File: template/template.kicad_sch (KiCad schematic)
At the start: 3 parts, among them J1 B2B STLink connector, U1 STM32G474RBT6

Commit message: Schematics for the first version of the STM32 template
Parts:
- added C1, C10, C11, C12, C14, C17, C3, C6, C9: 100n, symbol Device:C
- added C13: 4.7u, symbol Device:C
- added C15, C16: 30p, symbol Device:C
- added C2, C4, C5, C8: 1u, symbol Device:C
- added C7: 10n, symbol Device:C
- added D1: GREEN, symbol Device:LED
- added D2: YELLOW, symbol Device:LED
- added F1: 2A, symbol Device:Fuse
- added H1, H2, H3, H4: 2.7mm, MountingHole:MountingHole_2.7mm_Pad, symbol Mechanical:MountingHole_Pad
- added J1: Network Connector, symbol Exocet:Network_Connector
- added R2: 40, symbol Device:R
- added R3: 120, Resistor_THT:R_Axial_DIN0309_L9.0mm_D3.2mm_P12.70mm_Horizontal, symbol Device:R
- added R4: 80, symbol Device:R
- added R5: 10k, symbol Device:R
- added SW1: SW_Push, Button_Switch_THT:SW_PUSH_6mm, symbol Switch:SW_Push
- added TP1, TP2, TP3, TP4, TP5: TestPoint, TestPoint:TestPoint_Keystone_5005-5009_Compact, symbol Connector:TestPoint
- added U1: LD39050PU33R, Package_DFN_QFN:DFN-6-1EP_3x3mm_P0.95mm_EP1.7x2.6mm, symbol Exocet:LD39050PU33R
- added U3: SN65HVD230, Package_SO:SOIC-8_3.9x4.9mm_P1.27mm, symbol Interface_CAN_LIN:SN65HVD230
- added Y1: 8MHz, symbol Exocet:HSE_Oscillator
- J2: renamed from J1; footprint Exocet_Footprint:AVX 00-9159-010-BTB Connector -> Exocet:AVX 00-9159-010-BTB Connector; now not fitted
- R1: value 47Ω -> 47
- renumbered U1 to U2
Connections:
- net +3.3V: now also U2.1 (VBAT), U2.16 (VDD), U2.28 (VREF+), U2.29 (VDDA), U2.32 (VDD), U2.48 (VDD), U2.64 (VDD), C10.1, C11.1, C12.1, C13.1, C17.1, C2.2, C3.2, C5.1, C6.1, C7.1, C8.1, C9.1, R2.1, TP5.1, U1.4 (V_{out}), U3.3 (VCC)
- net GND: now also U2.15 (VSS), U2.27 (VSSA), U2.31 (VSS), U2.47 (VSS), U2.63 (VSS), C1.2, C10.2, C11.2, C12.2, C13.2, C14.1, C15.2, C16.2, C17.2, C2.1, C3.1, C4.2, C5.2, C6.2, C7.2, C8.2, C9.2, D1.1 (K), D2.1 (K), H1.1, H2.1, H3.1, H4.1, J1.5 (GND), R5.2, SW1.1, TP1.1, U1.2 (GND), U1.7 (GND), U3.2 (GND)
- net T_NRST: now also C14.2, SW1.2
- net CAN_RX: now reaches U2.45 (PA11)
- net CAN_RX: now also TP2.1, U3.4 (R)
- net CAN_TX: now reaches U2.46 (PA12)
- net CAN_TX: now also TP4.1, U3.1 (D)
- net OSC_IN: now reaches U2.5 (PF0)
- net OSC_IN: now also C15.1, Y1.1
- net OSC_OUT: now reaches U2.6 (PF1)
- net OSC_OUT: now also C16.1, Y1.2
- net STATUS_LED: now reaches U2.8 (PC0)
- net STATUS_LED: now also R4.1
- new net: F1.1, J1.2 (+5V)
- new net: D1.2 (A), R2.2
- new net: R5.1, U3.8 (Rs)
- new net: D2.2 (A), R4.2
- new net +24V: J1.1 (+24V)
- new net +5V: C1.1, C4.1, F1.2, TP3.1, U1.1 (EN), U1.6 (V_{in})
- new net CAN_H: J1.3 (CAN_H), R3.2, U3.7 (CANH)
- new net CAN_L: J1.4 (CAN_L), R3.1, U3.6 (CANL)
- no-connect marks 1 -> 43
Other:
- note added: "CAN Tranceiver"
- note added: "Mounting Holes"
- note added: "Network Connector"
- note added: "Oscillator"
- note added: "Reset Button"
- note added: "STLink"
- note added: "STM32"
- note added: "Status LEDs"
- note added: "Termination Resistor"
- note added: "Test Points"
- note added: "Voltage Regulator"
- moved on the sheet: R1, U2

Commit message: Add oscillator symbol
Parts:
- Y1: footprint (none) -> Exocet:Crystal_SMD_HC49-SD
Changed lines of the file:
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@@
 			)
 		)
-		(property "Footprint" ""
+		(property "Footprint" "Exocet:Crystal_SMD_HC49-SD"
 			(at 200.66 25.4 0)
 			(effects

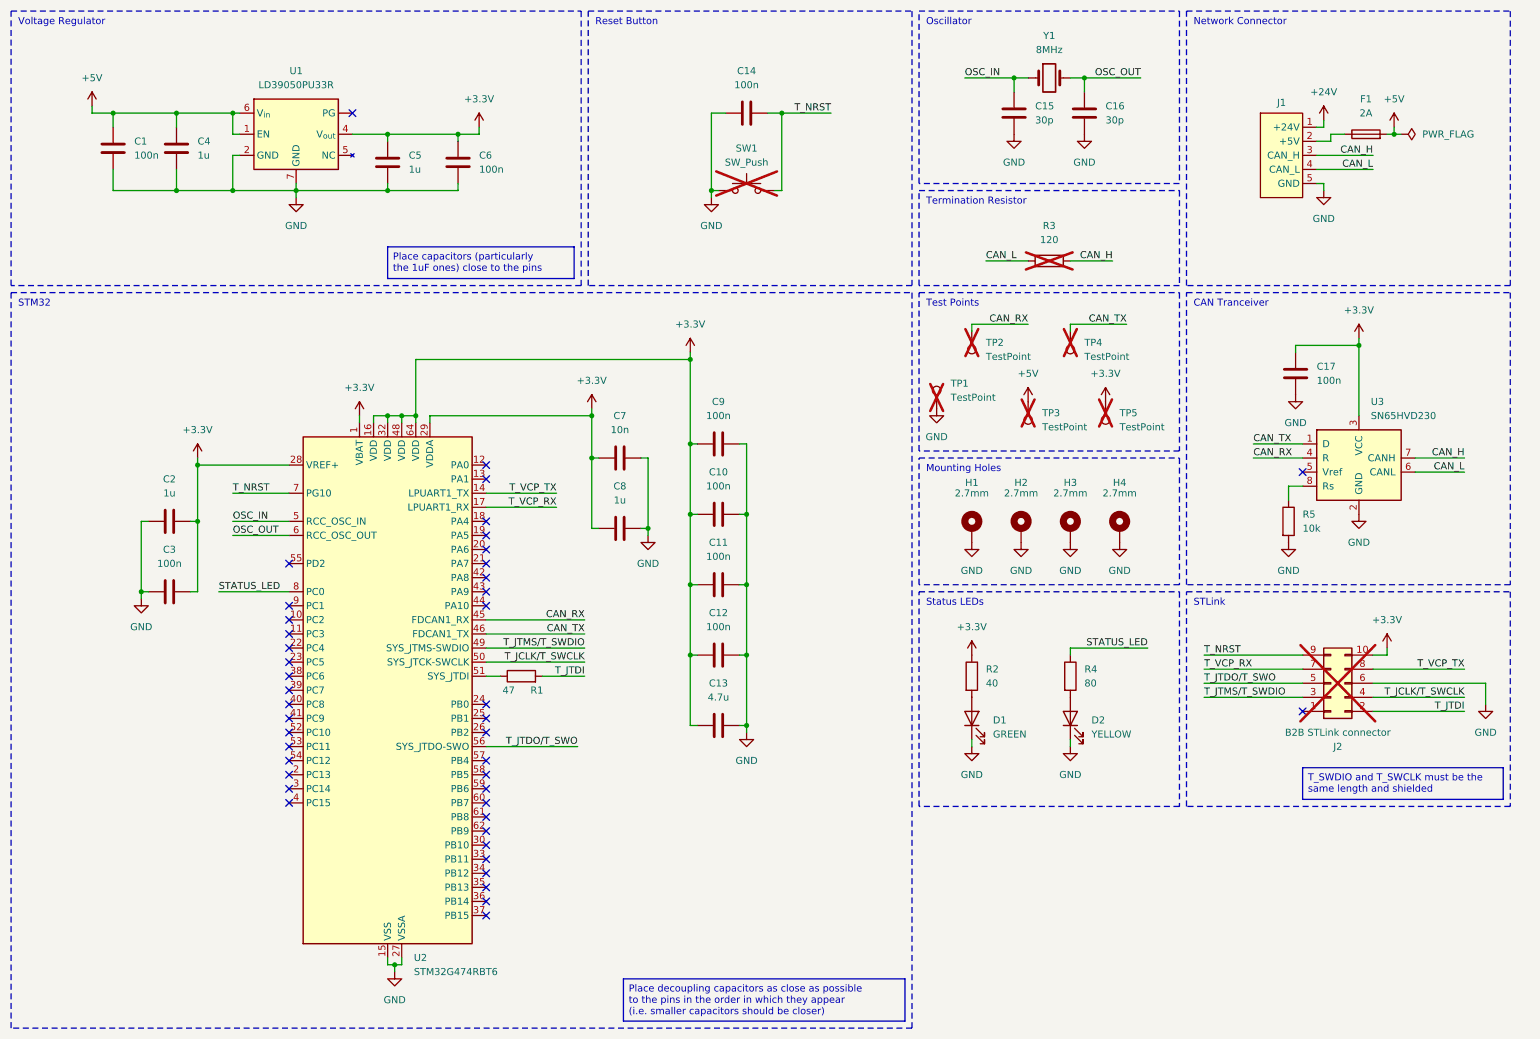
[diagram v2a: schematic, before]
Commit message: Footprints and part numbers
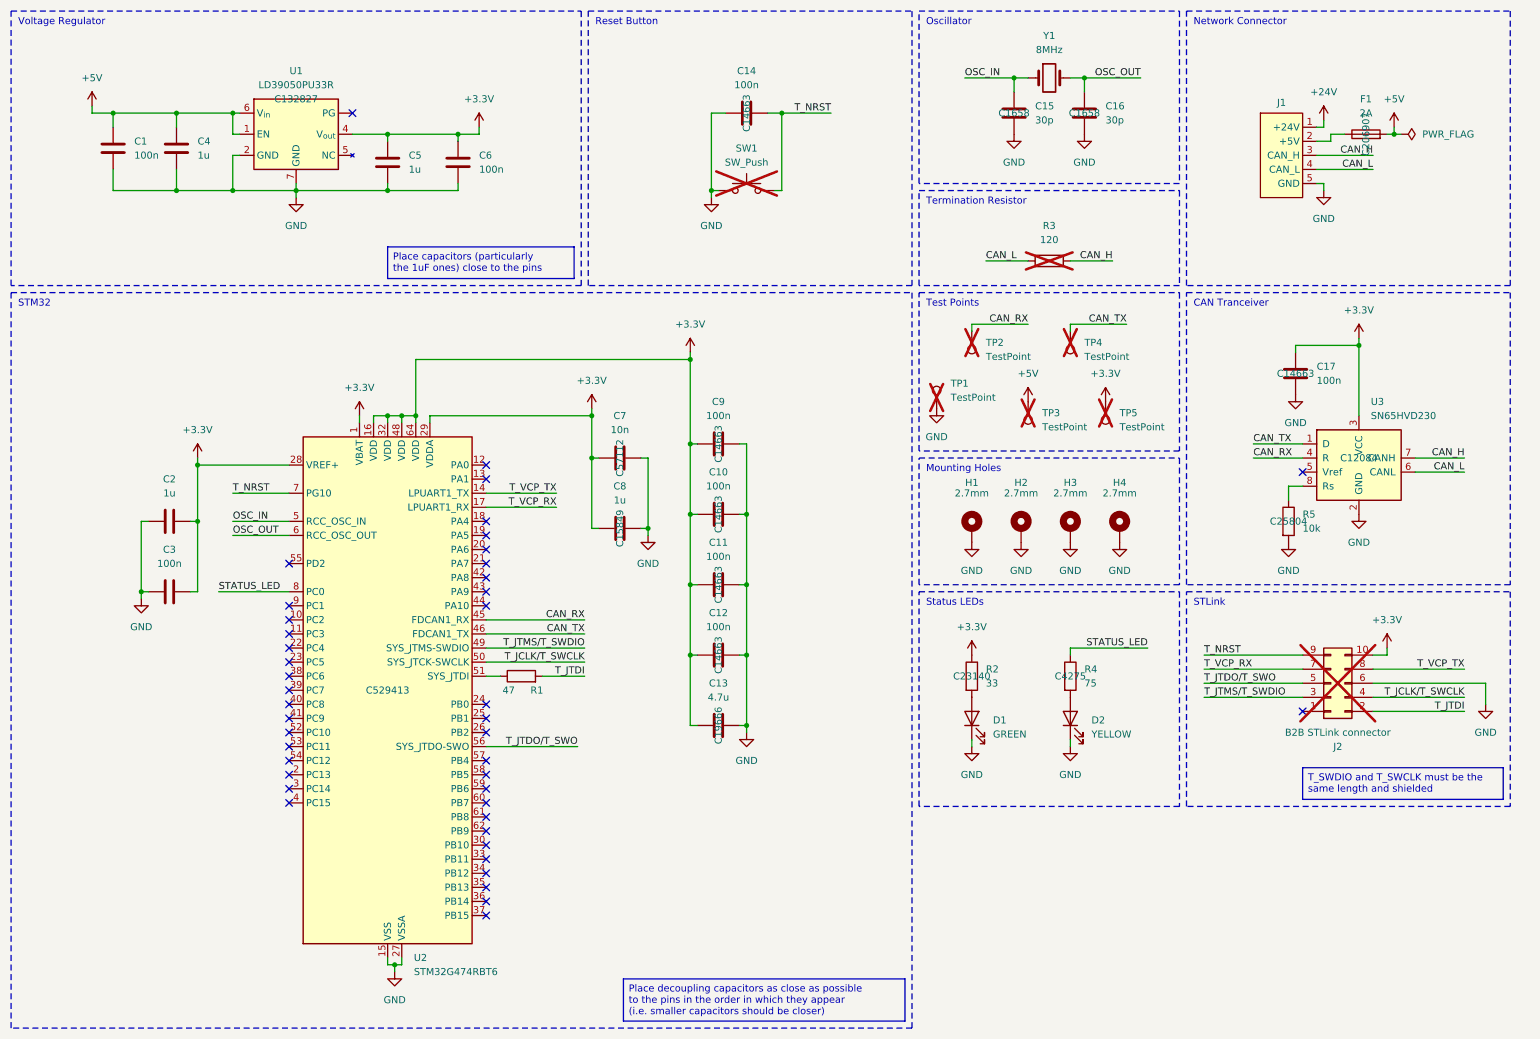
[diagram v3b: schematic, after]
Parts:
- C1, C10, C11, C12, C14, C17, C3, C6, C9: footprint (none) -> Capacitor_SMD:C_0603_1608Metric; JLCPCB (none) -> C14663
- C13: footprint (none) -> Capacitor_SMD:C_0603_1608Metric; JLCPCB (none) -> C19666
- C15, C16: footprint (none) -> Capacitor_SMD:C_0603_1608Metric; JLCPCB (none) -> C1658
- C2, C4, C5, C8: footprint (none) -> Capacitor_SMD:C_0603_1608Metric; JLCPCB (none) -> C15849
- C7: footprint (none) -> Capacitor_SMD:C_0603_1608Metric; JLCPCB (none) -> C57112
- D1: footprint (none) -> Exocet:LED_0805_2012Metric_With_Annotations; JLCPCB (none) -> C2297
- D2: footprint (none) -> Exocet:LED_0805_2012Metric_With_Annotations; JLCPCB (none) -> C2296
- F1: footprint (none) -> Exocet:Fuse_Holder_Littelfuse_01530008; JLCPCB (none) -> C206907
- J1: footprint (none) -> Connector_Molex:Molex_SPOX_5268-05A_1x05_P2.50mm_Horizontal; JLCPCB (none) -> C185201
- R1: footprint (none) -> Resistor_SMD:R_0603_1608Metric; JLCPCB (none) -> C23182
- R2: value 40 -> 33; footprint (none) -> Resistor_SMD:R_0603_1608Metric; JLCPCB (none) -> C23140
- R4: value 80 -> 75; footprint (none) -> Resistor_SMD:R_0603_1608Metric; JLCPCB (none) -> C4275
- R5: footprint (none) -> Resistor_SMD:R_0603_1608Metric; JLCPCB (none) -> C25804
- U1: JLCPCB (none) -> C132827
- U2: JLCPCB (none) -> C529413
- U3: JLCPCB (none) -> C12084

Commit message: Initial placement and routing
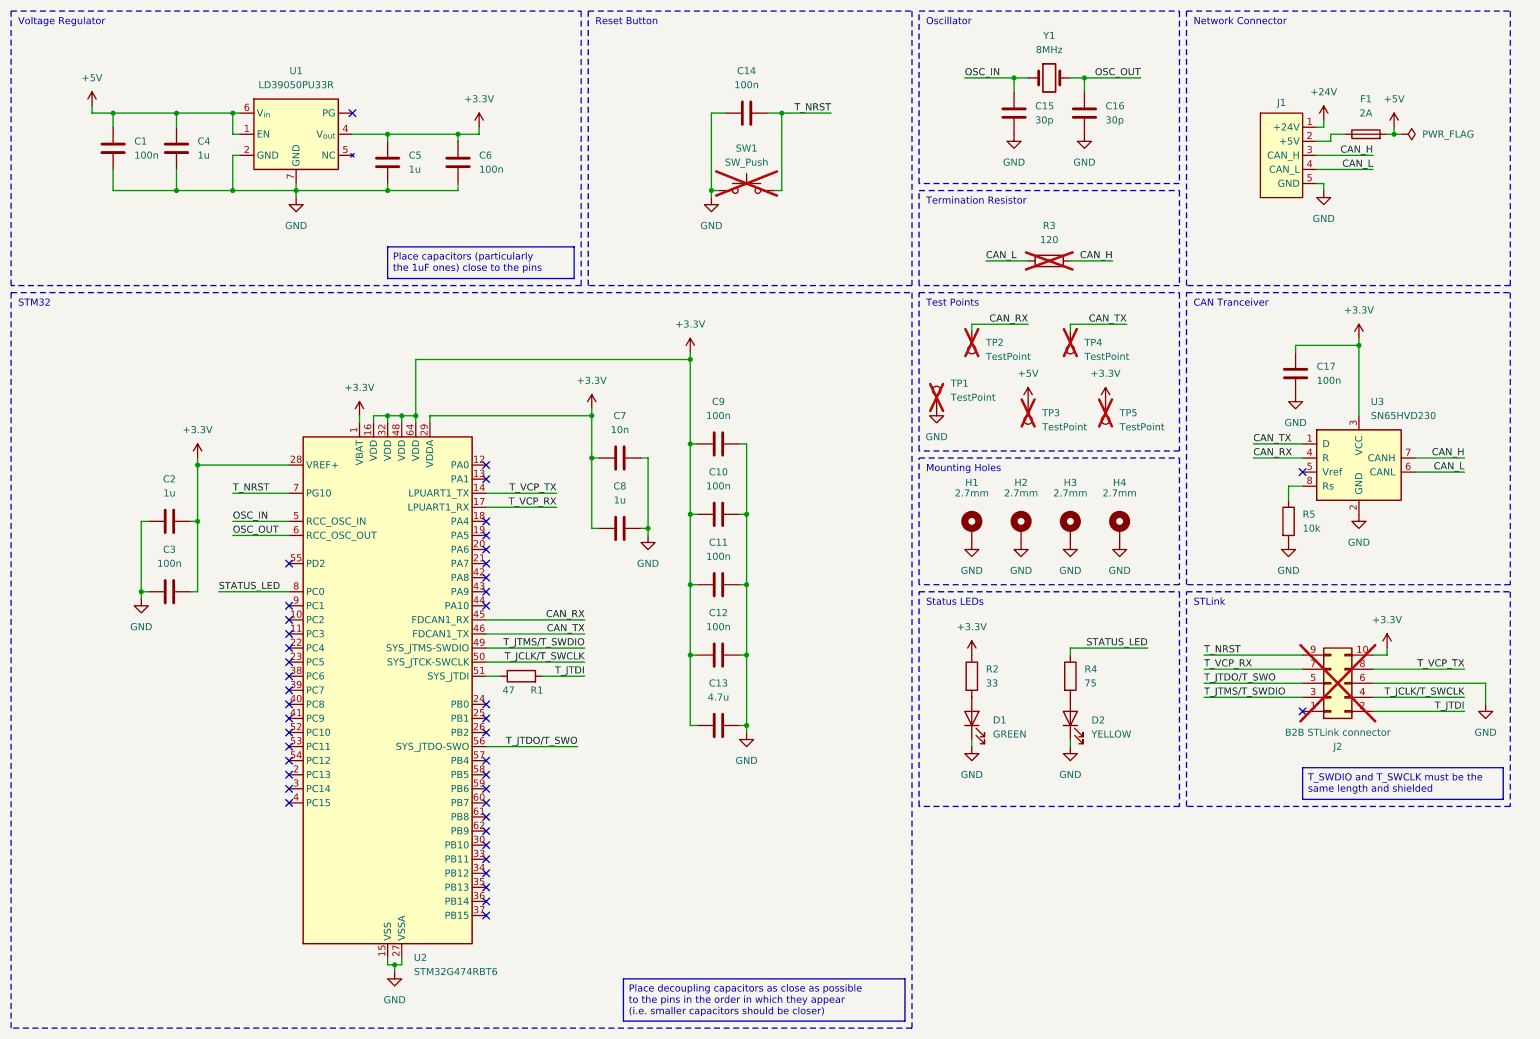
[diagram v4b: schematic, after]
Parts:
- C1, C10, C11, C12, C14, C17, C3, C6, C9: footprint Capacitor_SMD:C_0603_1608Metric -> Capacitor_SMD:C_0402_1005Metric; JLCPCB C14663 -> C1525
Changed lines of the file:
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@@
 					(size 1.27 1.27)
 				)
+				(hide yes)
 			)
 		)
@@
 					(size 1.27 1.27)
 				)
+				(hide yes)
 			)
 		)
@@
 					(size 1.27 1.27)
 				)
+				(hide yes)
 			)
 		)
@@
 			)
 		)
-		(property "Footprint" "Capacitor_SMD:C_0603_1608Metric"
+		(property "Footprint" "Capacitor_SMD:C_0402_1005Metric"
 			(at 45.72 117.1448 0)
 			(effects
@@
 			)
 		)
-		(property "JLCPCB" "C14663"
+		(property "JLCPCB" " C1525"
 			(at 41.91 118.11 0)
 			(effects
@@
 			)
 		)
-		(property "Footprint" "Capacitor_SMD:C_0603_1608Metric"
+		(property "Footprint" "Capacitor_SMD:C_0402_1005Metric"
 			(at 32.7152 41.91 0)
 			(effects
@@
 			)
 		)
-		(property "JLCPCB" "C14663"
+		(property "JLCPCB" " C1525"
 			(at 31.75 38.1 0)
 			(effects
@@
 					(size 1.27 1.27)
 				)
+				(hide yes)
 			)
 		)
@@
 					(size 1.27 1.27)
 				)
+				(hide yes)
 			)
 		)
@@
 			)
 		)
-		(property "Footprint" "Capacitor_SMD:C_0603_1608Metric"
+		(property "Footprint" "Capacitor_SMD:C_0402_1005Metric"
 			(at 144.78 115.8748 0)
 			(effects
@@
 			)
 		)
-		(property "JLCPCB" "C14663"
+		(property "JLCPCB" " C1525"
 			(at 140.97 116.84 0)
 			(effects
@@
 					(size 1.27 1.27)
 				)
+				(hide yes)
 			)
 		)
@@
 			)
 		)
-		(property "Footprint" "Capacitor_SMD:C_0603_1608Metric"
+		(property "Footprint" "Capacitor_SMD:C_0402_1005Metric"
 			(at 94.9452 44.45 0)
 			(effects
@@
 			)
 		)
-		(property "JLCPCB" "C14663"
+		(property "JLCPCB" " C1525"
 			(at 93.98 40.64 0)
 			(effects
@@
 					(size 1.27 1.27)
 				)
+				(hide yes)
 			)
 		)
@@
 					(size 1.27 1.27)
 				)
+				(hide yes)
 			)
 		)
@@
 					(size 1.27 1.27)
 				)
+				(hide yes)
 			)
 		)
@@
 			)
 		)
-		(property "Footprint" "Capacitor_SMD:C_0603_1608Metric"
+		(property "Footprint" "Capacitor_SMD:C_0402_1005Metric"
 			(at 144.78 103.1748 0)
 			(effects
@@
 			)
 		)
-		(property "JLCPCB" "C14663"
+		(property "JLCPCB" " C1525"
 			(at 140.97 104.14 0)
 			(effects
@@
 					(size 1.27 1.27)
 				)
+				(hide yes)
 			)
 		)
@@
 					(size 1.27 1.27)
 				)
+				(hide yes)
 			)
 		)
@@
 					(size 1.27 1.27)
 				)
+				(hide yes)
 			)
 		)
@@
 			)
 		)
-		(property "Footprint" "Capacitor_SMD:C_0603_1608Metric"
+		(property "Footprint" "Capacitor_SMD:C_0402_1005Metric"
 			(at 149.86 30.7848 0)
 			(effects
@@
 			)
 		)
-		(property "JLCPCB" "C14663"
+		(property "JLCPCB" " C1525"
 			(at 146.05 31.75 0)
 			(effects
@@
 					(size 1.27 1.27)
 				)
+				(hide yes)
 			)
 		)
@@
 					(size 1.27 1.27)
 				)
+				(hide yes)
 			)
 		)
@@
 			)
 		)
-		(property "Footprint" "Capacitor_SMD:C_0603_1608Metric"
+		(property "Footprint" "Capacitor_SMD:C_0402_1005Metric"
 			(at 246.0752 82.55 0)
 			(effects
@@
 			)
 		)
-		(property "JLCPCB" "C14663"
+		(property "JLCPCB" " C1525"
 			(at 245.11 78.74 0)
 			(effects
@@
 					(size 1.27 1.27)
 				)
+				(hide yes)
 			)
 		)
@@
 			)
 		)
-		(property "Footprint" "Capacitor_SMD:C_0603_1608Metric"
+		(property "Footprint" "Capacitor_SMD:C_0402_1005Metric"
 			(at 144.78 128.5748 0)
 			(effects
@@
 			)
 		)
-		(property "JLCPCB" "C14663"
+		(property "JLCPCB" " C1525"
 			(at 140.97 129.54 0)
 			(effects
@@
 					(size 1.27 1.27)
 				)
+				(hide yes)
 			)
 		)
@@
 			)
 		)
-		(property "Footprint" "Capacitor_SMD:C_0603_1608Metric"
+		(property "Footprint" "Capacitor_SMD:C_0402_1005Metric"
 			(at 144.78 90.4748 0)
 			(effects
@@
 			)
 		)
-		(property "JLCPCB" "C14663"
+		(property "JLCPCB" " C1525"
 			(at 140.97 91.44 0)
 			(effects
@@
 					(size 1.27 1.27)
 				)
+				(hide yes)
 			)
 		)
@@
 					(size 1.27 1.27)
 				)
+				(hide yes)
 			)
 		)

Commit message: Routing done
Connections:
- net CAN_H: now also J1.4 (CAN_H); no longer J1.3 (CAN_H)
- net CAN_L: now also J1.3 (CAN_L); no longer J1.4 (CAN_L)
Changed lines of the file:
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@@
-		)
-	)
-	(label "CAN_H"
-		(at 259.08 39.37 180)
-		(effects
-			(font
-				(size 1.27 1.27)
-			)
-			(justify right bottom)
 		)
 	)
@@
 		)
 	)
-	(label "CAN_L"
-		(at 259.08 41.91 180)
-		(effects
-			(font
-				(size 1.27 1.27)
-			)
-			(justify right bottom)
-		)
-	)
 	(label "T_JTDI"
 		(at 275.59 139.7 180)
@@
 		)
 	)
+	(label "CAN_H"
+		(at 259.08 41.91 180)
+		(effects
+			(font
+				(size 1.27 1.27)
+			)
+			(justify right bottom)
+		)
+	)
 	(label "OSC_OUT"
 		(at 217.17 25.4 180)
@@
 			)
 			(justify left bottom)
+		)
+	)
+	(label "CAN_L"
+		(at 259.08 39.37 180)
+		(effects
+			(font
+				(size 1.27 1.27)
+			)
+			(justify right bottom)
 		)
 	)
@@
 		(pin "1"
 		)
-		(pin ""
+		(pin "3"
 		)
 		(instances
